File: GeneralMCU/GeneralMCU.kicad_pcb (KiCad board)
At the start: 2 copper layers, 30 x 80 mm, 86 parts, among them J1 ARM_JTAG_SWD, J2 SMD castellation PKG, J3 USB_B_Micro, J5 PWR, J6 OLED, Q1 Q_NMOS_DGS, SW1 USER, SW2 RESET, U1 STM32F303R6Tx, U2 SN65HVD230, U3 AZ1117-3.3, U4 P78E05-1000, U5 DS18B20, Y1 32.768kHz, Y2 8MHz

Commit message: Can't remember these changes lol
From the meeting, switching back to branch now.
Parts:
- added snblock1: Logo_Open_Hardware_Small, µ104KiCAD:SN_BLOCK, B.Cu at (57.5, 87.5)
- added snblock2: Logo_Open_Hardware_Small, µ104KiCAD:SN_BLOCK, F.Cu at (55.8, 87.5)
- added snblock3: Logo_Open_Hardware_Small, µ104KiCAD:Paradigm_Logo_Very_Small, B.Cu at (72.2, 76.8)
- added snblock4: Logo_Open_Hardware_Small, µ104KiCAD:Paradigm_Logo_Very_Small, B.Cu at (73.8, 139.8)
- added snblock5: Logo_Open_Hardware_Small, Symbol:KiCad-Logo2_8mm_SilkScreen, B.Cu at (61.0, 115.2)
- added snblock6: Logo_Open_Hardware_Small, Symbol:ESD-Logo_6.6x6mm_SilkScreen, B.Cu at (70.5, 85.5)
- added snblock7: Logo_Open_Hardware_Small, Symbol:ESD-Logo_6.6x6mm_SilkScreen, F.Cu at (67.5, 124.0)
- added snblock8: Logo_Open_Hardware_Small, µ104KiCAD:Paradigm_Logo_Very_Small, F.Cu at (55.2, 91.2)
- renumbered JP1 to JP1-CANH, JP2 to JP2-CANL
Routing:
- net VBUS: track 9.33 -> 52.0 mm, vias 0 -> 4
- net /BUZZ: track 0.00 -> 36.3 mm, vias 0 -> 2
- net GND: track 79.9 -> 103.3 mm, vias 50 -> 55
- net /PC2: track 0.00 -> 21.7 mm, vias 1 -> 3
- net /PC3: track 0.00 -> 20.7 mm, vias 1 -> 3
- net /PA0: track 0.00 -> 18.7 mm, vias 1 -> 5
- net /USR_LED: track 11.7 -> 28.9 mm
- net /I2C1_SDA: track 30.7 -> 42.8 mm, vias 7 -> 8
- net /NRST: track 10.5 -> 18.8 mm, vias 1 -> 2
- net +5V: track 141.3 -> 148.8 mm
- net /I2C1_SCL: track 31.0 -> 36.9 mm, vias 7 -> 9
- net +3V3: track 143.2 -> 145.8 mm, vias 5 -> 7
- net Net-(D8-Pad2): track 0.00 -> 1.50 mm
- net /PC1: track 14.1 -> 15.6 mm, vias 4 -> 3
- net /PC11: track 30.5 -> 32.0 mm
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- added copper zone on F.Cu, net GND
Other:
- board text added: "(c) Paradigm Hyperloop GeneralMCU PCB PN: 2019-001 v1.0 SN:"
- board text added: "+5V"
- board text added: "+V"
- board text added: "3V3"
- board text added: "C10"
- board text added: "EXT PWR"
- board text added: "JTAG"
- board text added: "PCB #: 2019-001 Sch: Mitchell Stride Layout: Mitchell Stride BOM: Mitchell Stride Review:"
- board text added: "Paradigm Hyperloop IndicatorLEDs PCB"
- board text added: "RST"
- board text added: "USB"
- board text added: "USB PWR"
- board text added: "USR"

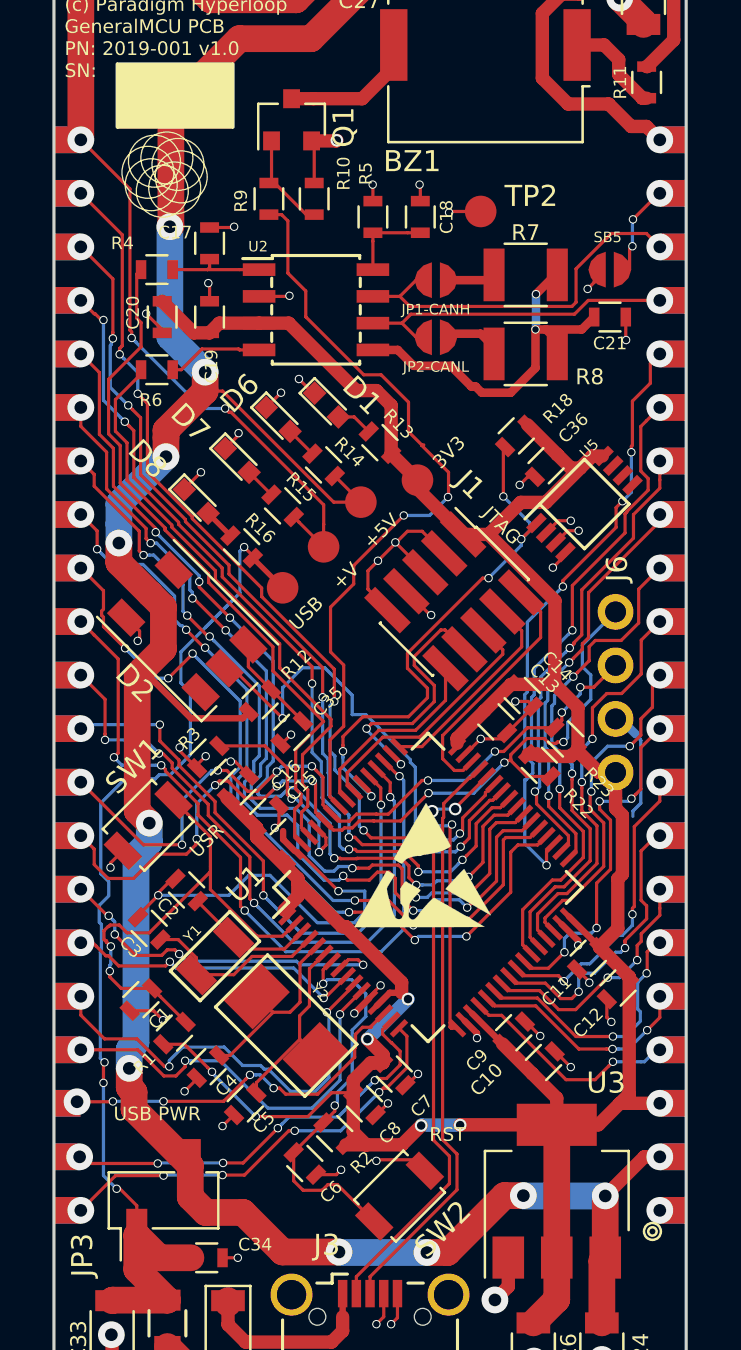
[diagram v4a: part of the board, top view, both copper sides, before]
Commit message: Fixed castellated pads. Ready for review
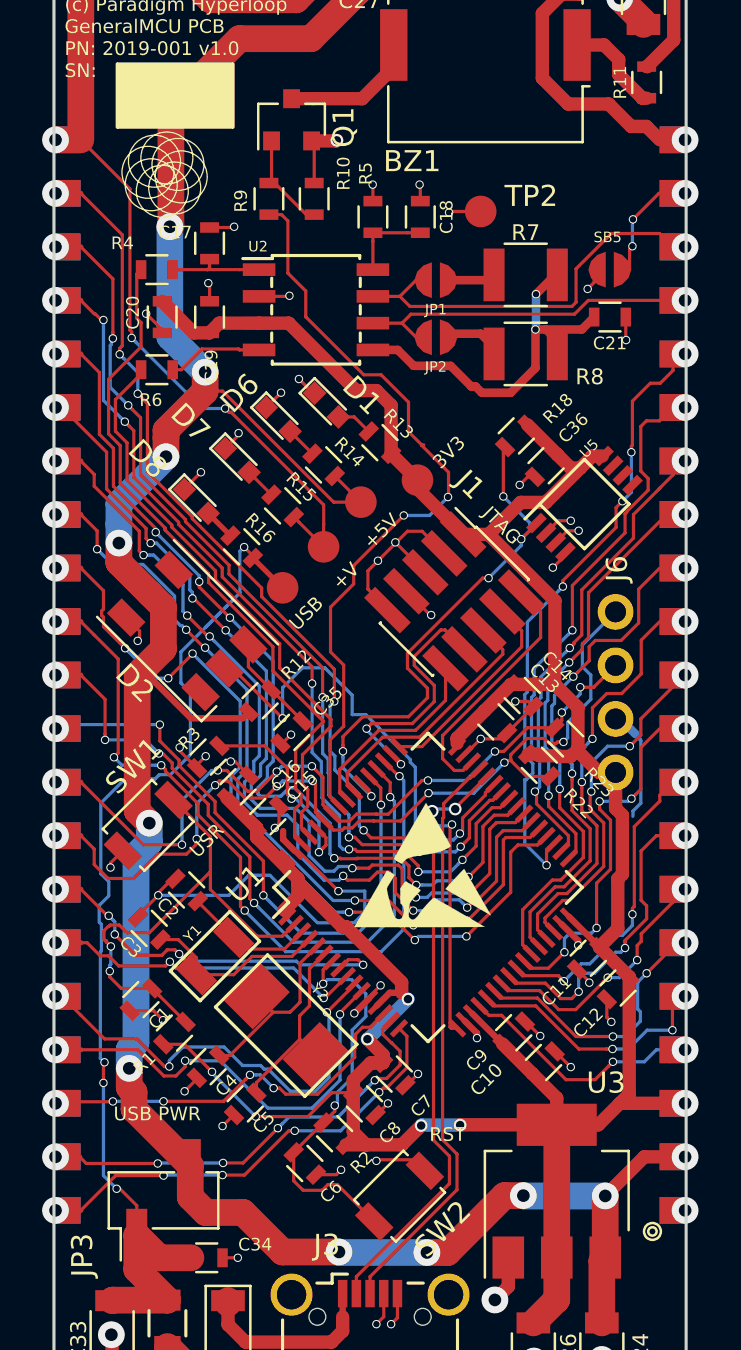
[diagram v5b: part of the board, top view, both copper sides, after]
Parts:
- removed snblock4: Logo_Open_Hardware_Small, µ104KiCAD:Paradigm_Logo_Very_Small
- F1: value 32VDC 1A PTC -> 3VDC 1A PTC
- snblock5: footprint Symbol:KiCad-Logo2_8mm_SilkScreen -> Symbol:KiCad-Logo_8mm_SilkScreen
- moved snblock5 37.7 mm to (61.5, 77.6), turned to 180 degrees
- moved snblock3 10.6 mm to (65.5, 84.9)
- moved snblock6 9.45 mm to (76.0, 77.8)
- renumbered JP1-CANH to JP1, JP2-CANL to JP2
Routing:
- net /PC12: track 29.3 -> 27.7 mm
- net GND: track 103.3 -> 102.1 mm
- net /PB14: track 28.9 -> 30.1 mm
- net /PA6: track 14.3 -> 13.2 mm
- net /PC2: track 21.7 -> 20.7 mm
- net /PC8: track 43.7 -> 42.6 mm
- net /CAN_Shield: track 4.79 -> 5.45 mm
- net /PC7: track 42.3 -> 41.7 mm
- net /PC6: track 39.8 -> 39.2 mm
- net /PC3: track 20.7 -> 20.1 mm
- net /PC0: track 18.2 -> 17.5 mm
- net /PB15: track 39.5 -> 38.9 mm
- net /PA9: track 43.9 -> 43.3 mm
- net /PA2: track 21.6 -> 21.0 mm
- net /PA10: track 45.3 -> 44.6 mm
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
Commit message: Added silk and generated gerbers. Review me.
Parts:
- added snblock10: Logo_Open_Hardware_Small, pics:stride, B.Cu at (74.6, 97.0)
- added snblock11: Logo_Open_Hardware_Small, pics:MUN, F.Cu at (71.7, 76.5)
- added snblock4: Logo_Open_Hardware_Small, pics:poddy, B.Cu at (62.0, 116.0)
- added snblock9: Logo_Open_Hardware_Small, pics:datboi, F.Cu at (70.3, 85.0)
- J2: value SMD castellation PKG -> SMD46 castellation PKG
- moved snblock1 58.5 mm to (75.5, 143.2), turned to 90 degrees
- moved snblock3 40.9 mm to (74.7, 124.8)
- moved R11 1.13 mm to (77.0, 86.6)
- moved snblock8 0.98 mm to (54.3, 91.3)
- moved C28 0.76 mm to (77.3, 82.3), turned to 90 degrees
- moved snblock2 0.60 mm to (56.4, 87.5)
- moved snblock7 0.40 mm to (67.3, 124.3), turned to 45 degrees
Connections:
- J2 pad 22: +V -> GND
- J2 pad 23: /PA10 -> Net-(J2-Pad23)
- J2 pad 24: /PA9 -> Net-(J2-Pad24)
- J2 pad 25: /PA8 -> GND
- J2 pad 26: /PC9 -> +V
- J2 pad 27: /PC8 -> /PA10
- J2 pad 28: /PC7 -> /PA9
- J2 pad 29: /PC6 -> /PA8
- J2 pad 30: /PB15 -> /PC9
- J2 pad 31: /PC10 -> /PC8
- J2 pad 32: /PC11 -> /PC7
- J2 pad 33: /PC12 -> /PC6
- J2 pad 34: /I2C1_SCL -> /PB15
- J2 pad 35: /I2C1_SDA -> /PC10
- J2 pad 36: /PC0 -> /PC11
- J2 pad 37: /PC1 -> /PC12
- J2 pad 38: /PC2 -> /I2C1_SCL
- J2 pad 39: /PC3 -> /I2C1_SDA
- J2 pad 40: /PA0 -> /PC0
- J2 pad 41: /PA1 -> /PC1
- J2 pad 42: /PA2 -> /PC2
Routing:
- net GND: track 102.1 -> 134.7 mm, vias 55 -> 78
- net +V: track 55.9 -> 57.6 mm
- net /PC7: track 41.7 -> 40.0 mm
- net /PB2: track 23.1 -> 24.8 mm
- net Net-(BZ1-Pad1): track 4.76 -> 3.16 mm
- net /PB14: track 30.1 -> 31.4 mm
- net /PC8: track 42.6 -> 41.4 mm
- net /PC12: track 27.7 -> 28.8 mm
- net /PB12: track 22.5 -> 23.5 mm
- net /PB10: track 18.9 -> 19.9 mm
- net /PB15: track 38.9 -> 39.7 mm
- net /PC6: track 39.2 -> 38.4 mm
- net /PB1: track 25.9 -> 26.6 mm
- net /PC9: track 43.7 -> 43.1 mm
- net Net-(J2-Pad23): track 0.00 -> 0.30 mm, vias 0 -> 1
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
